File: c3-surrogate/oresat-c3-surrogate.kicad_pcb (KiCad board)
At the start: 2 copper layers, 99.8 x 94.6 mm, 73 parts, among them J1 J-SAMTEC-TFM-120-X1-XXX-D-RA, J2 Conn_01x04, J4 PHOENIX_1995499, Q1 PMV45EN, Q3 NTR4101P, Q4 NTR4101P, Q5 DMP3050LVT-7, SW2 EG1218, SW3 OS203011MV9QS1, SW4 EG1218, U1 MAX892LEUA+T, U2 LTC4412xS6, U4 LTC4412xS6, U5 TS5A21366, U6 Trinket-M0

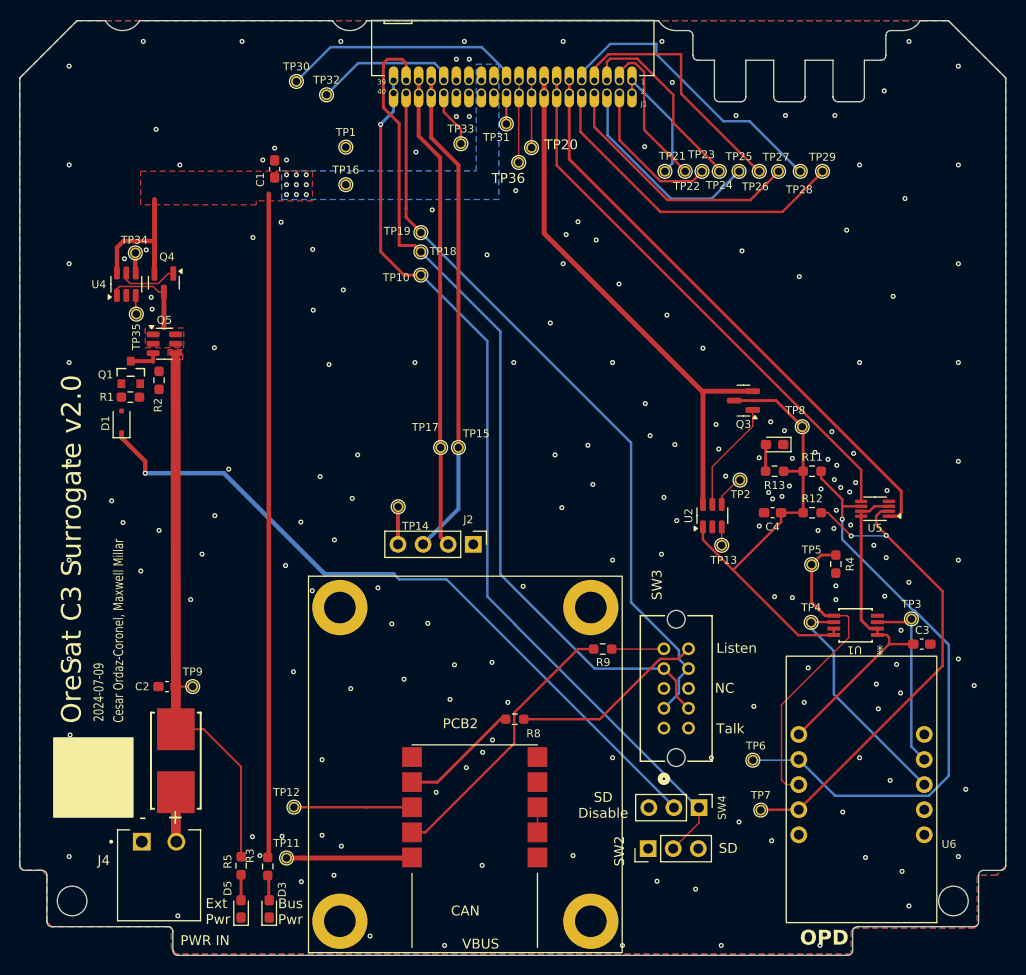
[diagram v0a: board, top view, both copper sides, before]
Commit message: removed VBUS zones, changed layout on right side of board
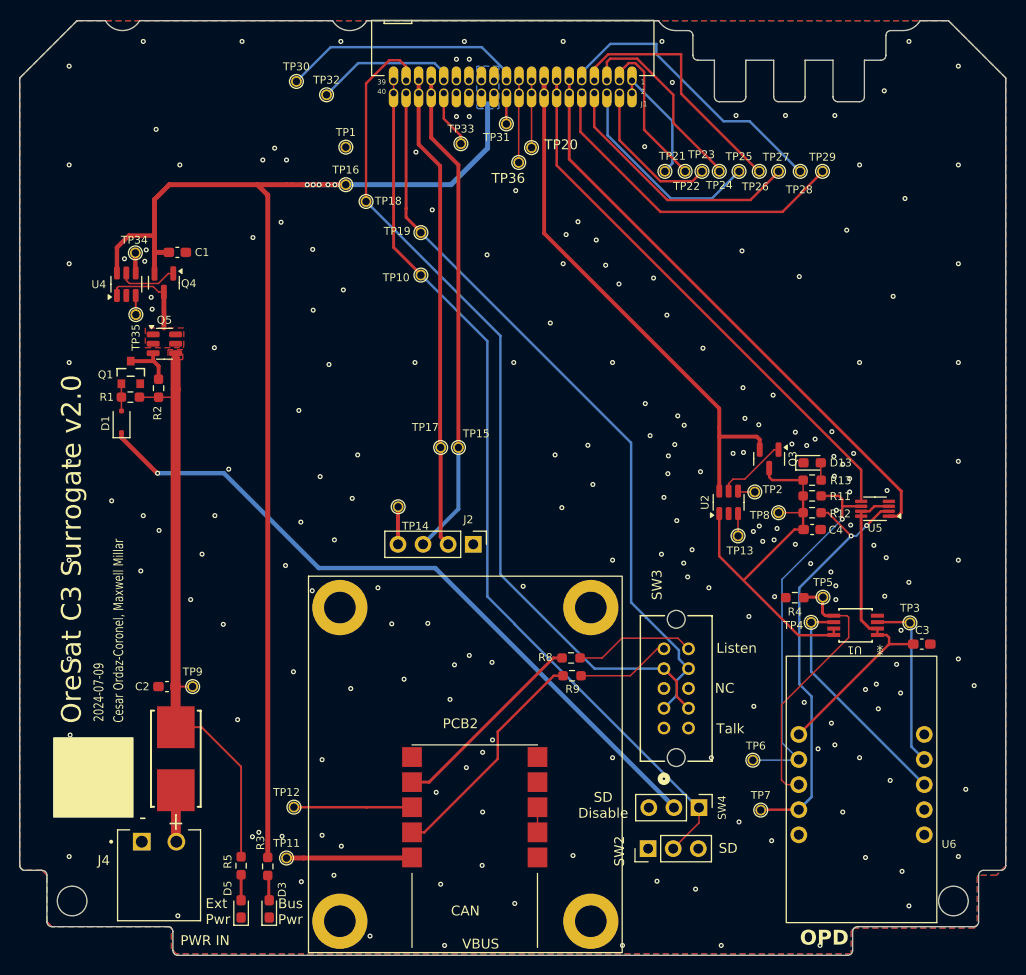
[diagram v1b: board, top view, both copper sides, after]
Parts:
- moved C1 13.0 mm to (116.0, 78.8), turned to 0 degrees
- moved TP8 9.02 mm to (176.8, 105.2)
- moved R8 8.42 mm to (155.8, 119.9)
- moved TP18 7.54 mm to (135.1, 73.7)
- moved Q3 6.45 mm to (175.8, 99.8), turned to -90 degrees
- moved R4 5.36 mm to (178.4, 113.8), turned to 180 degrees
- moved C4 4.35 mm to (180.2, 106.9), turned to 0 degrees
- moved D13 4.23 mm to (180.2, 100.2), turned to 0 degrees
- moved R9 4.11 mm to (155.9, 121.7)
- moved R13 3.91 mm to (180.2, 101.9), turned to 0 degrees
- moved TP5 3.49 mm to (181.3, 113.8)
- moved R11 2.50 mm to (180.2, 103.5)
- moved U2 2.13 mm to (171.8, 104.2)
- moved TP2 1.92 mm to (174.4, 103.1)
- moved TP13 1.90 mm to (172.7, 107.5)
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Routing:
- net VBUS: track 81.4 -> 129.2 mm, vias 9 -> 5
- net Net-(U5-COM2): track 60.6 -> 38.6 mm
- net Net-(Q3-D): track 48.1 -> 39.7 mm
- net Net-(PCB2-TXD): track 12.1 -> 20.4 mm
- net Net-(U5-COM1): track 51.3 -> 43.4 mm
- net Net-(R8-Pad2): track 19.6 -> 12.2 mm
- net /OPD_ISET: track 32.3 -> 27.6 mm
- net Net-(PCB2-RXD): track 27.9 -> 23.5 mm
- net Net-(R9-Pad2): track 5.30 -> 9.52 mm
- net Net-(Q3-G): track 11.4 -> 7.38 mm
- net Net-(Q5-S): track 57.5 -> 61.0 mm
- net Net-(Q1-D): track 3.13 -> 6.35 mm
- net Net-(D1-A): track 0.00 -> 2.76 mm
- net ~{SD}: track 93.8 -> 91.7 mm, vias 1 -> 0
- net Net-(U2-STAT): track 3.35 -> 1.74 mm
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- removed copper zone on F.Cu, net VBUS

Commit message: layout changes, labeled a couple test points
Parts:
- moved R9 2.45 mm to (155.8, 124.2)
- moved SW2 2.30 mm to (165.2, 140.9)
- moved SW4 2.12 mm to (170.2, 136.6)
- moved PCB2 0.95 mm to (151.4, 149.7)
- moved TP2 0.85 mm to (175.2, 103.5)
- moved U2 0.78 mm to (172.3, 104.7)
- moved TP11 0.75 mm to (127.8, 140.2)
- moved TP13 0.67 mm to (173.3, 107.8)
- moved TP15 0.30 mm to (144.4, 98.9)
- moved TP17 0.30 mm to (142.6, 98.9)
- moved TP8 0.25 mm to (177.1, 105.2)
- moved R3 0.15 mm to (125.2, 141.0)
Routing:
- net ~{SD}: track 91.7 -> 94.1 mm
- net Net-(D1-K): track 72.0 -> 74.1 mm
- net Net-(PCB2-RXD): track 23.5 -> 21.7 mm
- net Net-(PCB2-CTS#): track 12.7 -> 11.0 mm
- net Net-(R9-Pad2): track 9.52 -> 10.6 mm
- net Net-(Q3-D): track 39.7 -> 38.7 mm
- net Net-(PCB2-TXD): track 20.4 -> 21.3 mm
- net Net-(PCB2-RTS#): track 12.0 -> 11.0 mm
- net Net-(Q3-G): track 7.38 -> 6.87 mm
- net VBUS: track 129.2 -> 129.4 mm, vias 5 -> 6
- net GND: vias 208 -> 209
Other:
- board text added: "CAN1_H"
- board text added: "CAN1_L"
- board text added: "CTS"
- board text added: "RTS"

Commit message: Final layout polish and cleanup; no significant issues, just polishing.
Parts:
- moved TP16 20.9 mm to (112.4, 75.3)
- moved TP14 3.03 mm to (141.3, 105.0)
- moved J2 3.00 mm to (148.9, 108.4)
- moved R9 2.55 mm to (155.8, 121.6)
- moved TP36 2.55 mm to (150.5, 67.2)
- moved TP20 2.35 mm to (151.8, 65.9)
- moved Q3 2.22 mm to (173.6, 99.9), turned to 0 degrees
- moved C3 2.01 mm to (189.5, 117.6)
- moved TP6 1.60 mm to (175.8, 130.2)
- moved TP7 0.81 mm to (175.8, 135.2)
- moved TP3 0.75 mm to (190.1, 115.6)
- moved TP34 0.63 mm to (112.3, 79.1)
- moved U2 0.07 mm to (172.4, 104.7)
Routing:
- net Net-(Q3-D): track 38.7 -> 46.6 mm
- net Net-(Q4-D): track 9.80 -> 6.16 mm
- net OPD_PWR: track 54.3 -> 51.0 mm
- net /CAN2_L: track 8.30 -> 5.75 mm
- net /CAN2_H: track 6.79 -> 4.44 mm
- net Net-(PCB2-RXD): track 21.7 -> 23.6 mm
- net VBUS: track 129.4 -> 127.6 mm, vias 6 -> 0
- net Net-(U5-COM2): track 38.6 -> 37.0 mm
- net CAN1_L: track 48.2 -> 49.4 mm
- net Net-(Q3-G): track 6.87 -> 5.65 mm
- net CAN1_H: track 49.6 -> 48.4 mm
- net Net-(R9-Pad2): track 10.6 -> 9.58 mm
- net /SPARE21: track 24.6 -> 25.6 mm
- net /OPD_~{ENABLE}: track 17.8 -> 18.8 mm
- net Net-(U1-IN): track 34.0 -> 34.8 mm
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- added copper zone on F.Cu, net VBUS
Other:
- board text added: "Bus"
- board text added: "C3-UART-RX"
- board text added: "C3-UART-TX"
- board text added: "Ext"
- board text added: "~{SD}"
- board text removed: "Bus Pwr"
- board text removed: "Ext Pwr"
- board text removed: "PWR IN"

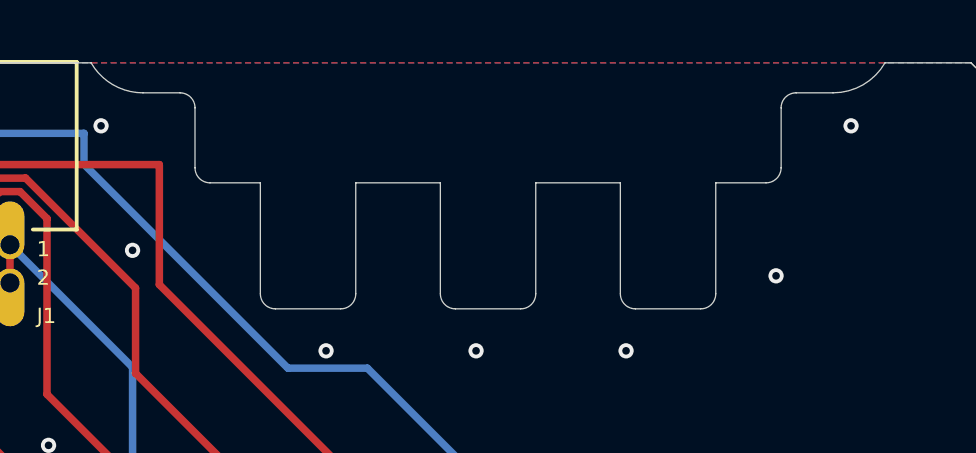
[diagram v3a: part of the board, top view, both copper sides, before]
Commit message: Updates for v2 production run, including BOM changes, and polishing of symbols
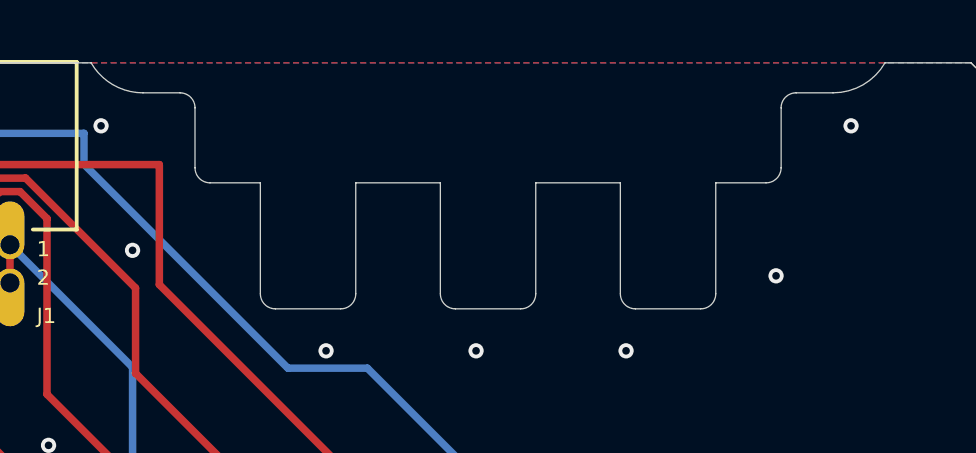
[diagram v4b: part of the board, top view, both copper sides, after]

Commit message: More polishing, along with library cleanup
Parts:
- removed U6: Trinket-M0, oresat-mcu:Adafruit-Trinket
- added PCB3: Trinket-M0, oresat-pcbs:Adafruit-Trinket, F.Cu at (185.2, 132.7)
- J4: value PHOENIX_1995499 -> 1995499
- PCB2: footprint oresat-misc:UMFT234XF -> oresat-pcbs:UMFT234XF
- U1: footprint oresat-passives:MAX892 -> oresat-ics:LINEAR-MSOP-8-AND-MAXIM-UMAX-8-21-0036
